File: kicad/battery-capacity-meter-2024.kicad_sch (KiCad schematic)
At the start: 58 parts, among them J1 PWR, J2 GND, J3 Conn_MainBoard, J4 Conn_DisplayBoard, Q1 2N3904, Q2 2N3906, Q3 2SD2390, SW1 SW_CHARGE/DISCHARGE, SW2 1A MODE, U1 LM2596_StepDown_Module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

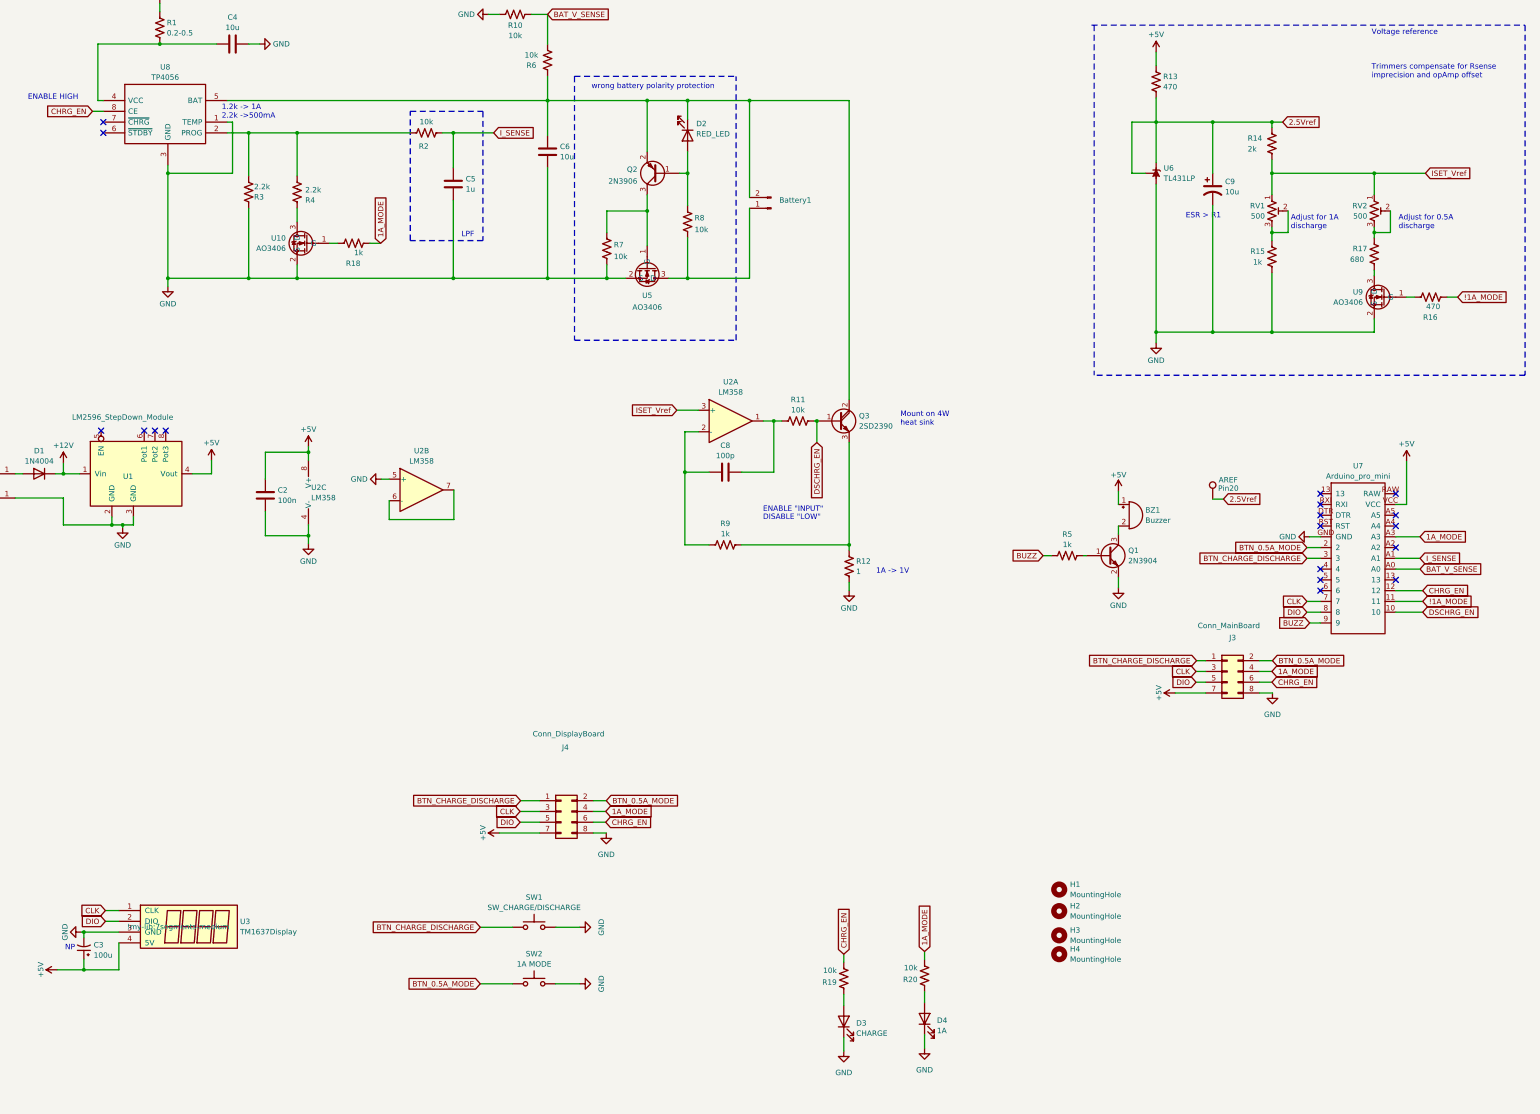
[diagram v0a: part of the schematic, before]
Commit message: hardware-ok. firware barelly workin
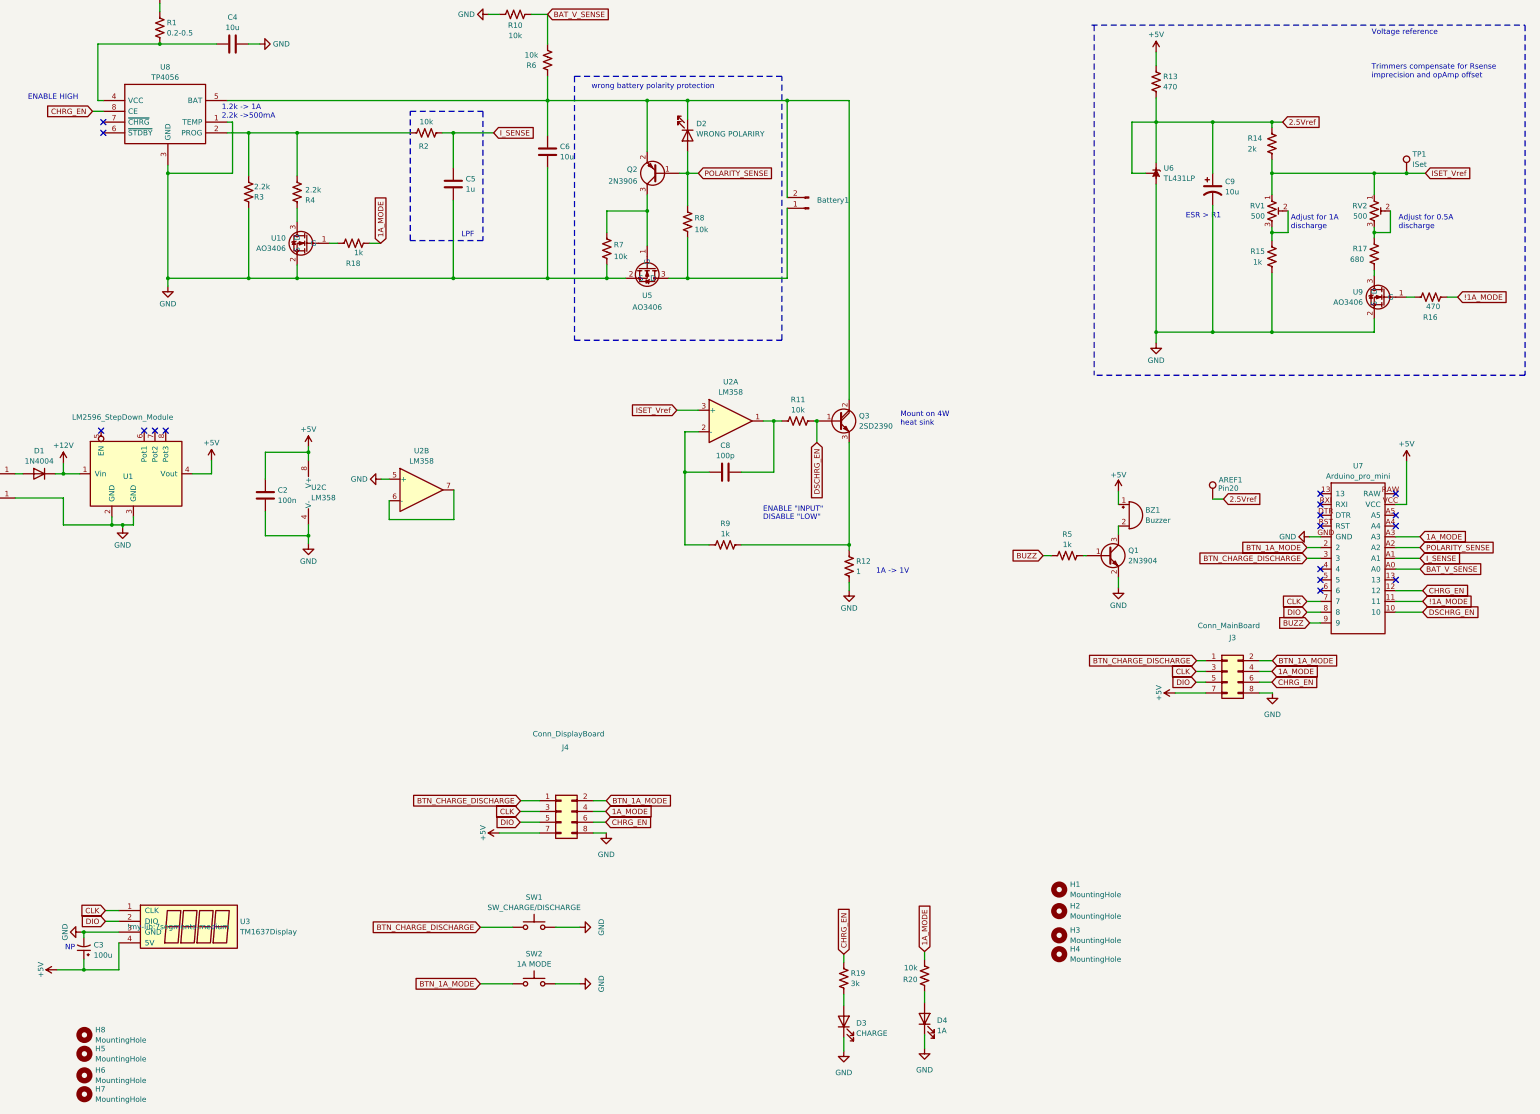
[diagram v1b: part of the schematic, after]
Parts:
- added H5, H6, H7, H8: MountingHole, MountingHole:MountingHole_2.2mm_M2, symbol Mechanical:MountingHole
- added TP1: ISet, Connector_Wire:SolderWire-0.5sqmm_1x01_D0.9mm_OD2.1mm, symbol Connector:TestPoint
- D2: value RED_LED -> WRONG POLARIRY
- R19: value 10k -> 3k
- renumbered AREF to AREF1
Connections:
- net ISET_Vref: now also TP1.1
- net POLARITY_SENSE: now reaches D2.2 (A), Q2.1 (B), R8.2
- net POLARITY_SENSE: now also U7.A2
- net BTN_0.5A_MODE renamed BTN_1A_MODE
- no-connect marks 18 -> 17
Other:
- moved on the sheet: Battery1

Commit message: working v1
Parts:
- added R21: 10k, Resistor_SMD:R_0805_2012Metric, symbol Device:R_US
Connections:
- net POLARITY_SENSE: now also R21.2; no longer D2.2 (A), Q2.1 (B), R8.2
- net at Battery1.1 (Pin_1), R8.1, U5.3 (D): now also R21.1
- new net: D2.2 (A), Q2.1 (B), R8.2
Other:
- moved on the sheet: D2
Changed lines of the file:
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@@
   (junction (at 303.53 97.79) (diameter 0) (color 0 0 0 0)
   )
+  (junction (at 202.565 85.09) (diameter 0) (color 0 0 0 0)
+  )
   (junction (at 354.965 74.295) (diameter 0) (color 0 0 0 0)
   )
@@
     (stroke (width 0) (type default))
   )
-  (polyline (pts (xy 215.265 99.695) (xy 215.265 37.465))
+  (polyline (pts (xy 213.995 93.98) (xy 213.995 37.465))
     (stroke (width 0) (type dot))
   )
@@
     (stroke (width 0) (type default))
   )
-  (polyline (pts (xy 166.37 37.465) (xy 166.37 99.695))
+  (polyline (pts (xy 165.1 37.465) (xy 165.1 93.98))
     (stroke (width 0) (type dot))
   )
@@
     (stroke (width 0) (type default))
   )
-  (wire (pts (xy 193.04 55.245) (xy 193.04 60.325))
+  (wire (pts (xy 193.04 52.705) (xy 193.04 60.325))
     (stroke (width 0) (type default))
   )
@@
     (stroke (width 0) (type default))
   )
+  (wire (pts (xy 191.77 102.235) (xy 202.565 102.235))
+    (stroke (width 0) (type default))
+  )
   (wire (pts (xy 222.885 118.745) (xy 223.52 118.745))
     (stroke (width 0) (type default))
@@
     (stroke (width 0) (type default))
   )
+  (wire (pts (xy 202.565 85.09) (xy 216.535 85.09))
+    (stroke (width 0) (type default))
+  )
   (wire (pts (xy 300.99 60.325) (xy 297.815 60.325))
     (stroke (width 0) (type default))
@@
     (stroke (width 0) (type default))
   )
-  (polyline (pts (xy 166.37 99.695) (xy 215.265 99.695))
+  (polyline (pts (xy 165.1 93.98) (xy 213.995 93.98))
     (stroke (width 0) (type dot))
   )
@@
     (stroke (width 0) (type default))
   )
+  (wire (pts (xy 202.565 102.235) (xy 202.565 85.09))
+    (stroke (width 0) (type default))
+  )
   (wire (pts (xy 85.725 48.26) (xy 85.725 60.325))
     (stroke (width 0) (type default))
@@
     (stroke (width 0) (type default))
   )
-  (wire (pts (xy 193.04 85.09) (xy 216.535 85.09))
+  (wire (pts (xy 193.04 85.09) (xy 202.565 85.09))
     (stroke (width 0) (type default))
   )
@@
     (stroke (width 0) (type default))
   )
+  (wire (pts (xy 181.61 102.235) (xy 184.15 102.235))
+    (stroke (width 0) (type default))
+  )
   (wire (pts (xy 137.922 141.986) (xy 122.682 141.986))
     (stroke (width 0) (type default))
@@
     (stroke (width 0) (type dot))
   )
-  (wire (pts (xy 193.04 43.18) (xy 193.04 47.625))
+  (wire (pts (xy 193.04 43.18) (xy 193.04 45.085))
     (stroke (width 0) (type default))
   )
@@
     (stroke (width 0) (type default))
   )
-  (wire (pts (xy 193.04 60.325) (xy 195.58 60.325))
-    (stroke (width 0) (type default))
-  )
   (wire (pts (xy 173.863 208.28) (xy 170.815 208.28))
     (stroke (width 0) (type default))
@@
     )
   )
-  (global_label "POLARITY_SENSE" (shape input) (at 195.58 60.325 0) (fields_autoplaced)
-    (effects (font (size 1.27 1.27)) (justify left))
-    (property "Intersheetrefs" "${INTERSHEET_REFS}" (at 214.2285 60.325 0)
-      (effects (font (size 1.27 1.27)) (justify left) hide)
+  (global_label "POLARITY_SENSE" (shape input) (at 181.61 102.235 180) (fields_autoplaced)
+    (effects (font (size 1.27 1.27)) (justify right))
+    (property "Intersheetrefs" "${INTERSHEET_REFS}" (at 162.9615 102.235 0)
+      (effects (font (size 1.27 1.27)) (justify right) hide)
     )
   )
@@
   )
   (symbol (lib_id "Device:R_US") (at 193.04 71.755 180) (unit 1)
-    (in_bom yes) (on_board yes) (dnp no) (fields_autoplaced)
+    (in_bom yes) (on_board yes) (dnp no)
     (property "Reference" "R8" (at 194.691 70.8465 0)
       (effects (font (size 1.27 1.27)) (justify right))
@@
     )
   )
-  (symbol (lib_id "Device:LED") (at 193.04 51.435 270) (unit 1)
+  (symbol (lib_id "Device:LED") (at 193.04 48.895 270) (unit 1)
     (in_bom yes) (on_board yes) (dnp no) (fields_autoplaced)
-    (property "Reference" "D2" (at 195.072 48.6354 90)
+    (property "Reference" "D2" (at 195.072 46.0954 90)
       (effects (font (size 1.27 1.27)) (justify left))
     )
-    (property "Value" "WRONG POLARIRY" (at 195.072 51.0596 90)
+    (property "Value" "WRONG POLARIRY" (at 195.072 48.5196 90)
       (effects (font (size 1.27 1.27)) (justify left))
     )
-    (property "Footprint" "LED_THT:LED_D5.0mm" (at 193.04 51.435 0)
+    (property "Footprint" "LED_THT:LED_D5.0mm" (at 193.04 48.895 0)
       (effects (font (size 1.27 1.27)) hide)
     )
-    (property "Datasheet" "~" (at 193.04 51.435 0)
+    (property "Datasheet" "~" (at 193.04 48.895 0)
       (effects (font (size 1.27 1.27)) hide)
     )
@@
   (symbol (lib_id "Connector:Conn_01x02_Pin") (at 221.615 68.58 180) (unit 1)
     (in_bom yes) (on_board yes) (dnp no)
-    (property "Reference" "Battery1" (at 227.33 66.675 0)
+    (property "Reference" "Battery1" (at 220.98 72.39 0)
       (effects (font (size 1.27 1.27)))
     )
@@
         )
       )
+    )
+  )
+  (symbol (lib_id "Device:R_US") (at 187.96 102.235 270) (unit 1)
+    (in_bom yes) (on_board yes) (dnp no)
+    (property "Reference" "R21" (at 190.4365 100.286 90)
+      (effects (font (size 1.27 1.27)) (justify right))
+    )
+    (property "Value" "10k" (at 190.4365 97.5109 90)
+      (effects (font (size 1.27 1.27)) (justify right))
+    )
+    (property "Footprint" "Resistor_SMD:R_0805_2012Metric" (at 187.706 103.251 90)
+      (effects (font (size 1.27 1.27)) hide)
+    )
+    (property "Datasheet" "~" (at 187.96 102.235 0)
+      (effects (font (size 1.27 1.27)) hide)
+    )
+    (pin "1")
+    (pin "2")
+    (instances
+      (project "battery-capacity-meter-2024"
+        (path "/e63e39d7-6ac0-4ffd-8aa3-1841a4541b55"
+          (reference "R21") (unit 1)
+        )
+      )

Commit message: add ovp
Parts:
- removed D2: WRONG POLARIRY, LED_THT:LED_D5.0mm, symbol Device:LED
- added C1: 47n, Capacitor_SMD:C_1206_3216Metric, symbol Device:C
- added D5: 1N4734A 5.6V, Diode_THT:D_DO-35_SOD27_P5.08mm_Vertical_KathodeUp, symbol Device:D_Zener
- added F1: 2A, Resistor_THT:R_Axial_DIN0309_L9.0mm_D3.2mm_P2.54mm_Vertical, symbol Device:Fuse
- added Q6: X0402MF, Package_TO_SOT_THT:TO-220-3_Vertical, symbol Triac_Thyristor:X0202NN
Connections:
- net POLARITY_SENSE: now also R21.1, C1.1, D5.2 (A), Q6.3 (G); no longer R21.2
- net at Battery1.1 (Pin_1), R8.1, U5.3 (D): now also R21.2, C1.2, Q6.1 (K); no longer R21.1
- net at C6.1, Q2.2 (E), Q3.2 (C)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: now also D5.1 (K), F1.1, Q6.2 (A), Q6.4 (A); no longer Battery1.2 (Pin_2)
- new net: Battery1.2 (Pin_2), F1.2
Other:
- note added: "Overvoltage protection"
- moved on the sheet: Battery1, C8, Q2, Q3, R11, R12, R21, R7, R8, R9, U2A, U2B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

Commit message: add overvoltage protection in hardware and cycle modes in firmware
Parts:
- removed F1: 2A, Resistor_THT:R_Axial_DIN0309_L9.0mm_D3.2mm_P2.54mm_Vertical, symbol Device:Fuse
- added D2, D6: 1N4148, Diode_SMD:D_MiniMELF, symbol Diode:1N4148
- added D7, D9: BAT54S, Package_TO_SOT_SMD:SOT-23, symbol Diode:BAT54S
- added R22, R24, R25: 10k, Resistor_SMD:R_0805_2012Metric, symbol Device:R_US
- added R23: 0.1, Resistor_SMD:R_2512_6332Metric, symbol Device:R_US
- added R26: 150, Resistor_SMD:R_0805_2012Metric, symbol Device:R_US
- added R27: 1M, Resistor_SMD:R_0805_2012Metric, symbol Device:R_US
- added TH1, TH2: 1A, !my-lib:PTC_1A_radial, symbol Device:Thermistor_PTC_US
- Battery1: footprint Connector_Phoenix_MC_HighVoltage:PhoenixContact_MCV_1,5_2-G-5.08_1x02_P5.08mm_Vertical -> Connector_JST:JST_VH_B2P-VH-B_1x02_P3.96mm_Vertical
- C1: value 47n -> 10n
- D5: value 1N4734A 5.6V -> 1N4732A 4.7V; footprint Diode_THT:D_DO-35_SOD27_P5.08mm_Vertical_KathodeUp -> Diode_SMD:D_MiniMELF
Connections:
- net +5V: now also D7.2 (K), D9.2 (K)
- net 2.5Vref: now also R25.1
- net GND: now also D7.1 (A), D9.1 (A), R26.2, R27.2; no longer U2.5 (+)
- net POLARITY_SENSE: now also D9.3 (COM), R22.2; no longer C1.1, D5.2 (A), Q6.3 (G), R21.1
- net at Battery1.1 (Pin_1), C1.2, R21.2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: now also R22.1, R23.2; no longer Q6.1 (K)
- net at C6.1, D5.1 (K), Q2.2 (E)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: now also D2.1 (K), TH1.1, TH2.1
- net at U2.6 (-): now also R25.2, R26.1; no longer U2.7
- net at Battery1.2 (Pin_2): now also TH1.2, TH2.2
- net at Q2.1 (B), R8.2: now also D2.2 (A)
- net OVP_SENSE: now reaches U7.4
- net OVP_SENSE: now also U2.7
- new net: C1.1, D6.1 (K), Q6.3 (G), R21.1
- new net: D5.2 (A), D6.2 (A)
- new net: D7.3 (COM), R24.2, R27.1, U2.5 (+)
- new net: Q6.1 (K), R23.1, R24.1
- no-connect marks 17 -> 16
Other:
- note added: "HI when SCR triggers"
- note added: "HI when wrong polarity"
- moved on the sheet: AREF1, BZ1, Battery1, C1, C2, C3, C4, C5, C6, C8, C9, D1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

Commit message: before tracks reset
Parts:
- removed J1: PWR, Connector_Wire:SolderWire-1.5sqmm_1x01_D1.7mm_OD3.9mm, symbol Connector:Conn_01x01_Socket
- removed J2: GND, Connector_Wire:SolderWire-1.5sqmm_1x01_D1.7mm_OD3.9mm, symbol Connector:Conn_01x01_Socket
- added J5: PWR, Connector_JST:JST_XH_B2B-XH-A_1x02_P2.50mm_Vertical, symbol Connector:Conn_01x02_Pin
- SW1: value SW_CHARGE/DISCHARGE -> CHARGE/DISCHARGE
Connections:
- net GND: now also J5.2 (Pin_2)
- net at D1.2 (A): now also J5.1 (Pin_1)
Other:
- note added: "drain some leakage voltage"
- moved on the sheet: D1, R25, R26, U1
